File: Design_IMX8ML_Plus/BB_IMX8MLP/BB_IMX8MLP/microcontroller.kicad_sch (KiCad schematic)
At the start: 0 parts

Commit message: Review
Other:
- note added: "Memeoria EEPROM PWM CAN I2C SPI UART"
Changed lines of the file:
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@@
 	(generator_version "8.0")
 	(paper "A4")
+	(text "Memeoria EEPROM\nPWM \nCAN\nI2C\nSPI\nUART"
+		(exclude_from_sim no)
+		(at 72.136 56.642 0)
+		(effects
+			(font
+				(size 5 5)
+			)
+		)
+	)
 )

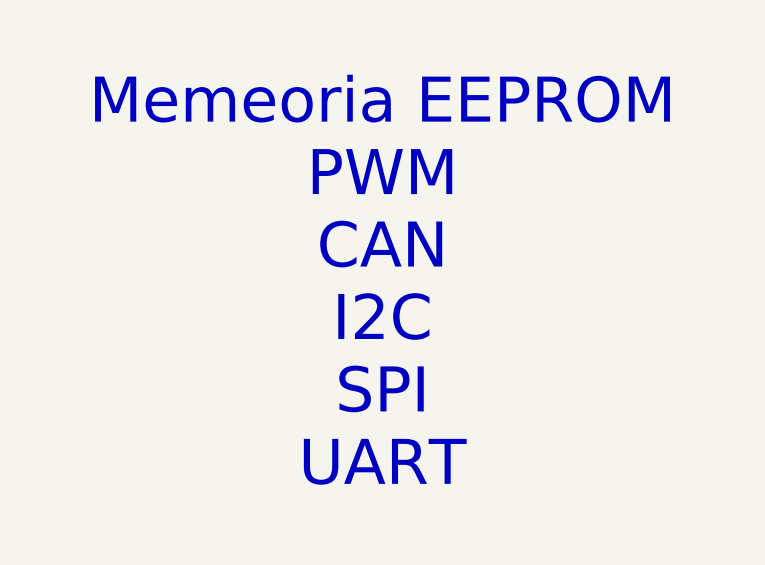
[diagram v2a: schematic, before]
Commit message: reorganization of the componentes
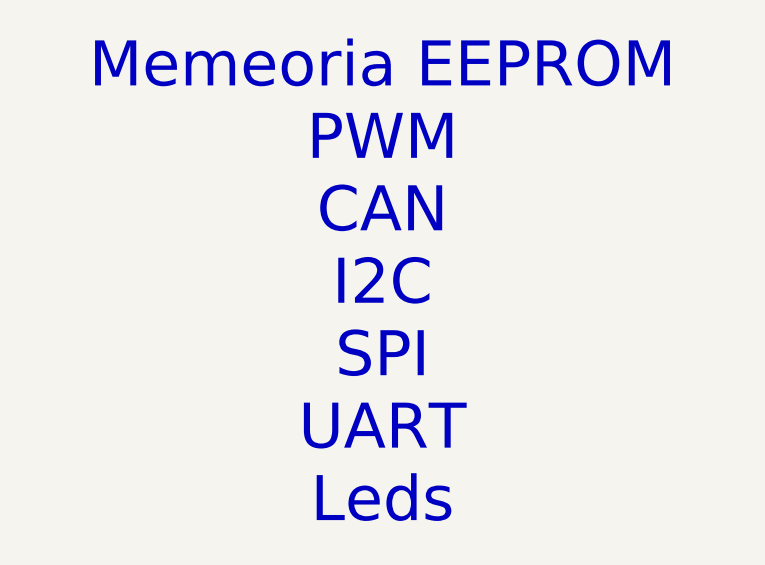
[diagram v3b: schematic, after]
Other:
- note added: "Memeoria EEPROM PWM CAN I2C SPI UART Leds"
- note removed: "Memeoria EEPROM PWM CAN I2C SPI UART"
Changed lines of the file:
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@@
 	(generator_version "8.0")
 	(paper "A4")
-	(text "Memeoria EEPROM\nPWM \nCAN\nI2C\nSPI\nUART"
+	(text "Memeoria EEPROM\nPWM \nCAN\nI2C\nSPI\nUART\nLeds"
 		(exclude_from_sim no)
 		(at 72.136 56.642 0)

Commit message: CPU Board actualizate
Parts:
- added C189, C190, C191, C192: 12Pf, Capacitor_SMD:C_0402_1005Metric, symbol Device:C_Small
- added C193: 100nF, Capacitor_SMD:C_0402_1005Metric, symbol Device:C_Small
- added J16: PB0, Connector_PinHeader_2.54mm:PinHeader_2x10_P2.54mm_Vertical, symbol Connector_Generic:Conn_02x10_Odd_Even
- added R82, R83: 100K, Resistor_SMD:R_0402_1005Metric, symbol Device:R_Small
- added SW4: NRST, Button_Switch_SMD:SW_SPST_TL3342, symbol Switch:SW_Push_Dual
- added SW5: BOOT0, Button_Switch_SMD:SW_SPST_TL3342, symbol Switch:SW_Push_Dual
- added U26: STM32H523CCUx, Package_DFN_QFN:QFN-48-1EP_7x7mm_P0.5mm_EP5.6x5.6mm, symbol MCU_ST_STM32H5:STM32H523CCUx
- added U27: CAT250xxx-HU4, Package_DFN_QFN:DFN-8-1EP_3x2mm_P0.5mm_EP1.75x1.45mm, symbol Memory_EEPROM:CAT250xxx-HU4
- added Y4, Y5: 25MHz, Crystal:Crystal_SMD_0603-4Pin_6.0x3.5mm, symbol Device:Crystal_GND24_Small
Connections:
- new net: C189.1, Y4.1
- new net: C191.1, Y5.1
- new net: C192.1, Y5.3
- new net: U27.4 (GND), U27.9 (GND)
- new net: SW5.1, SW5.3
- new net: U26.24 (VDD), U26.48 (VDD)
- new net: C193.1, R82.2, SW4.1, SW4.3
- new net: C190.1, Y4.3
- new net BOOT0: R83.1, SW5.2, SW5.4, U26.44 (BOOT0)
- new net GND: C189.2, C190.2, C191.2, C192.2, C193.2, R83.2, U26.23 (VSS), U26.35 (VSS), U26.47 (VSS), U26.49 (VSS), U26.8 (VSSA), Y4.2, Y4.4, Y5.2, Y5.4
- new net NRST: SW4.2, SW4.4, U26.7 (NRST)
- new net PB0: J16.4 (Pin_4), U26.18 (PB0)
- new net PB1: J16.3 (Pin_3), U26.19 (PB1)
- new net PB10: J16.14 (Pin_14), U26.21 (PB10)
- new net PB12: J16.16 (Pin_16), U26.25 (PB12)
- new net PB13: J16.15 (Pin_15), U26.26 (PB13)
- new net PB14: J16.18 (Pin_18), U26.27 (PB14)
- new net PB15: J16.17 (Pin_17), U26.28 (PB15)
- new net PB2: J16.6 (Pin_6), U26.20 (PB2)
- new net PB3: J16.5 (Pin_5), U26.39 (PB3(JTDO)
- new net PB4: J16.8 (Pin_8), U26.40 (PB4(NJTRST))
- new net PB5: J16.7 (Pin_7), U26.41 (PB5)
- new net PB6: J16.10 (Pin_10), U26.42 (PB6)
- new net PB7: J16.9 (Pin_9), U26.43 (PB7)
- new net PB8: J16.12 (Pin_12), U26.45 (PB8)
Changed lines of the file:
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@@
 	(generator_version "8.0")
 	(paper "A4")
-	(text "Memeoria EEPROM\nPWM \nCAN\nI2C\nSPI\nUART\nLeds"
-		(exclude_from_sim no)
-		(at 72.136 56.642 0)
-		(effects
-			(font
-				(size 5 5)
-			)
-		)
-	)
-)

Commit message: [PROCESSOR] Create zones It added power zones in the four layer
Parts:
- added J3: boot, Connector_PinHeader_2.54mm:PinHeader_1x04_P2.54mm_Vertical_SMD_Pin1Right, symbol Connector_Generic:Conn_02x02_Odd_Even
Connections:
- net GND: now also J16.19 (Pin_19), J16.20 (Pin_20)
- net at U26.12 (PA2): now also J3.1 (Pin_1)
- net at U26.13 (PA3): now also J3.3 (Pin_3)
- net jtag_Rx: now reaches U26.30 (PA9)
- net jtag_Tx: now reaches U26.31 (PA10)
- net USB_D-: now reaches U26.32 (PA11)
- net USB_D+: now reaches U26.33 (PA12)
- new net boot_Rx: J3.2 (Pin_2)
- new net boot_Tx: J3.4 (Pin_4)

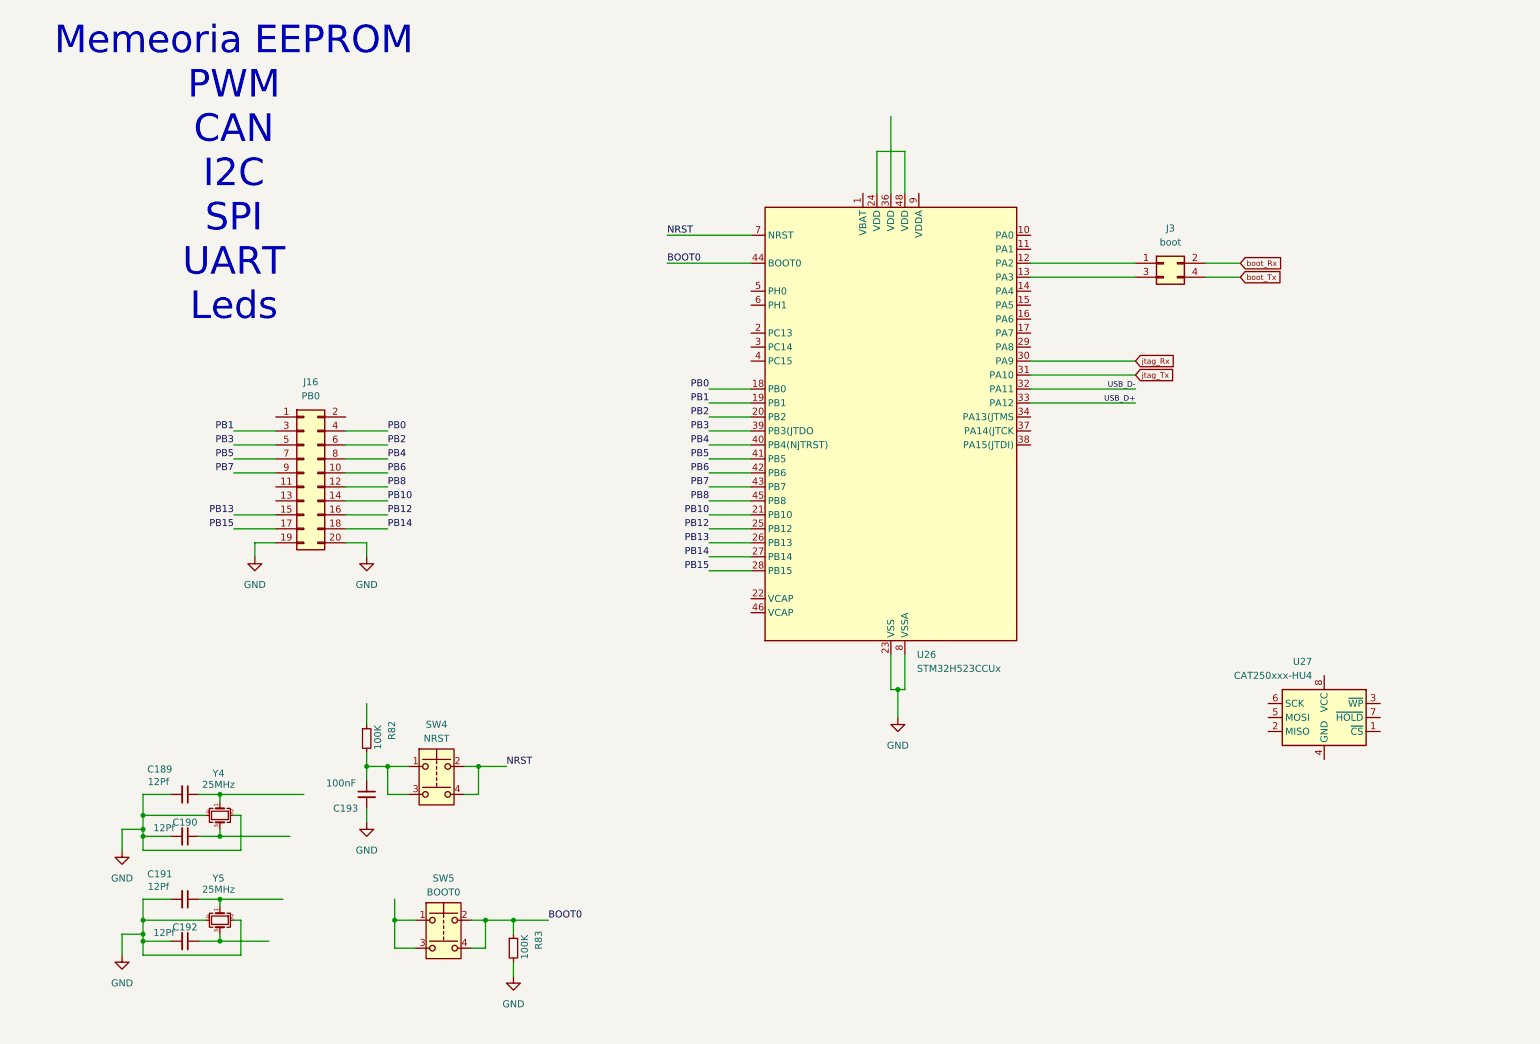
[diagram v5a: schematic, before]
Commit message: [BB_IMX8MLP IMX8MLP] Actuallizated to 9.0 kicad version
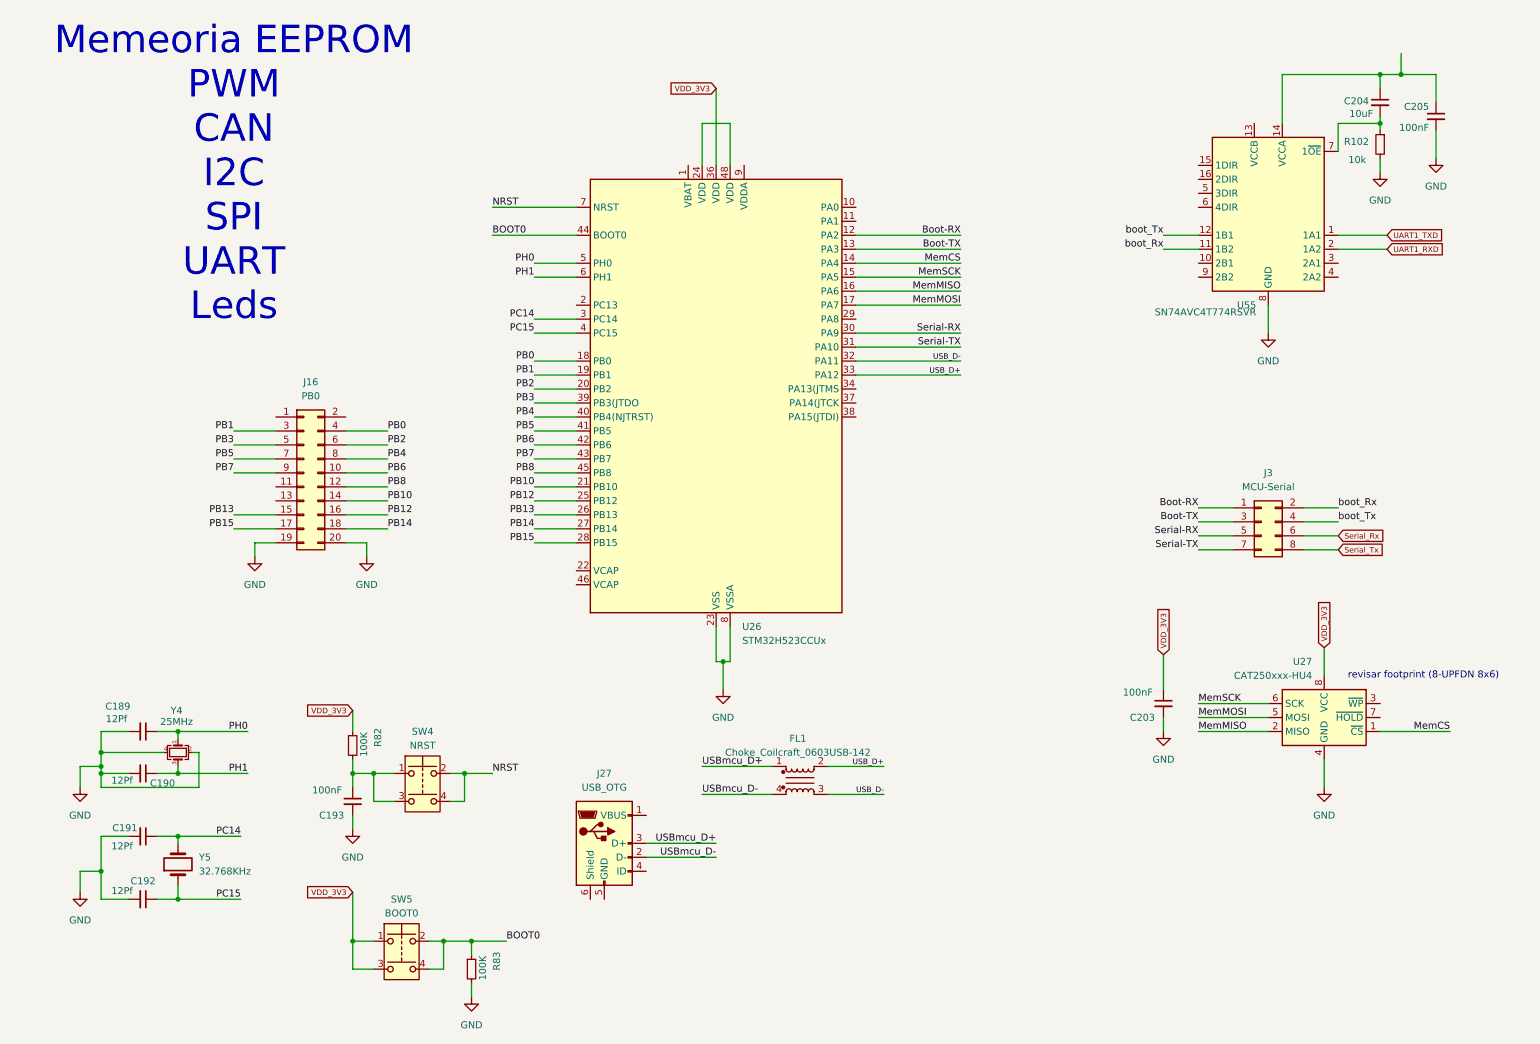
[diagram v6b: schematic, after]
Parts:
- removed J3: boot, Connector_PinHeader_2.54mm:PinHeader_1x04_P2.54mm_Vertical_SMD_Pin1Right, symbol Connector_Generic:Conn_02x02_Odd_Even
- removed Y5: 25MHz, Crystal:Crystal_SMD_0603-4Pin_6.0x3.5mm, symbol Device:Crystal_GND24_Small
- added C203, C205: 100nF, Capacitor_SMD:C_0402_1005Metric, symbol Device:C_Small
- added C204: 10uF, Capacitor_SMD:C_0402_1005Metric, symbol Device:C_Small
- added FL1: Choke_Coilcraft_0603USB-142, Inductor_SMD:L_CommonModeChoke_Coilcraft_0603USB, symbol Filter:Choke_Coilcraft_0603USB-142
- added J27: USB_OTG, Connector_USB:USB_Mini-B_Lumberg_2486_01_Horizontal, symbol Connector:USB_OTG
- added J3: MCU-Serial, Connector_PinHeader_2.54mm:PinHeader_2x04_P2.54mm_Vertical, symbol Connector_Generic:Conn_02x04_Odd_Even
- added R102: 10k, Resistor_SMD:R_0402_1005Metric, symbol Device:R_Small
- added U55: SN74AVC4T774RSVR, Package_DFN_QFN:UQFN-16_1.8x2.6mm_P0.4mm, symbol _W_MX8M:SN74AVC4T774RSVR
- added Y5: 32.768KHz, Crystal:Crystal_SMD_3215-2Pin_3.2x1.5mm, symbol Device:Crystal
- C189, C190, C191, C192: MP (none) -> C0402C120D5GACTU; Price (none) -> 0.5
- C193: MP (none) -> C0402C104K4RACTU; Price (none) -> 0.1
- R82, R83: MP (none) -> RC0402JR-07100KL; Price (none) -> 0.1
- U26: MP (none) -> STM32H523CCU6; Price (none) -> 4.5
- U27: MP (none) -> MT29F4G01ABAFDWB-IT:F TR; Price (none) -> 4
- Y4: footprint Crystal:Crystal_SMD_0603-4Pin_6.0x3.5mm -> Crystal:Crystal_SMD_3225-4Pin_3.2x2.5mm; MP (none) -> TSX-3225 25.0000MF15X-AS3; Price (none) -> 1.5
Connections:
- net GND: now also U27.4 (GND), U27.9 (GND), C203.2, C205.2, R102.2, U55.8 (GND)
- net USB_D+: now also FL1.2
- net USB_D-: now also FL1.3
- net boot_Rx: now also J3.2 (Pin_2), U55.11 (1B2)
- net boot_Tx: now also J3.4 (Pin_4), U55.12 (1B1)
- net PH0: now reaches C189.1, Y4.1
- net PH0: now also U26.5 (PH0)
- net PC14: now reaches C191.1
- net PC14: now also U26.3 (PC14), Y5.2
- net PC15: now reaches C192.1
- net PC15: now also U26.4 (PC15), Y5.1
- net MemCS: now reaches U27.1 (~{CS})
- net MemCS: now also U26.14 (PA4)
- net MemMISO: now reaches U27.2 (MISO)
- net MemMISO: now also U26.16 (PA6)
- net MemMOSI: now reaches U27.5 (MOSI)
- net MemMOSI: now also U26.17 (PA7)
- net MemSCK: now reaches U27.6 (SCK)
- net MemSCK: now also U26.15 (PA5)
- net VDD_3V3: now reaches U27.8 (VCC)
- net VDD_3V3: now also R82.1, SW5.1, SW5.3, U26.36 (VDD), C203.1
- net Boot-RX: now reaches U26.12 (PA2)
- net Boot-RX: now also J3.1 (Pin_1)
- net Boot-TX: now reaches U26.13 (PA3)
- net Boot-TX: now also J3.3 (Pin_3)
- net PH1: now reaches U26.6 (PH1)
- net PH1: now also C190.1, Y4.3
- net jtag_Rx renamed Serial-RX
- net Serial-RX: now also J3.5 (Pin_5)
- net jtag_Tx renamed Serial-TX
- net Serial-TX: now also J3.7 (Pin_7)
- new net: C204.1, C205.1, U55.14 (VCCA)
- new net: C204.2, R102.1, U55.7 (1~{OE})
- new net Serial_Rx: J3.6 (Pin_6)
- new net Serial_Tx: J3.8 (Pin_8)
- new net UART1_RXD: U55.2 (1A2)
- new net UART1_TXD: U55.1 (1A1)
- new net USBmcu_D+: FL1.1, J27.3 (D+)
- new net USBmcu_D-: FL1.4, J27.2 (D-)
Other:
- note added: "revisar footprint (8-UPFDN 8x6)"
- moved on the sheet: C189, C190, C191, C192, C193, R82, R83, SW4, SW5, U26, Y4
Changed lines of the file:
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@@
 (kicad_sch
-	(version 20231120)
+	(version 20250114)
 	(generator "eeschema")
-	(generator_version "8.0")
+	(generator_version "9.0")
 	(paper "A4")

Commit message: [LoRa] Starting a new project
Starting a new project base on LoRa LR1121, this project use
the module LBAA0XV2GT-001 that had sub-GHz and 2.4GHz frequencies.
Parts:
- removed FL1: Choke_Coilcraft_0603USB-142, Inductor_SMD:L_CommonModeChoke_Coilcraft_0603USB, symbol Filter:Choke_Coilcraft_0603USB-142
- added U57: PCMF1USB3SZ, _W_SBC:WLCSP52-1-2_NEX, symbol _W_MX8M:PCMF1HDMI2S
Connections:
- net GND: now also J27.5 (GND), U57.B1 (GND_CH1)
- net USB_D+: now also U57.C1 (CH1_OUT+)
- net USB_D-: now also U57.C2 (CH1_OUT-)
- net USBmcu_D+: now also U57.A1 (CH1_IN+)
- net USBmcu_D-: now also U57.A2 (CH1_IN-)
- net boot_Tx: no longer U55.12 (1B1)
- new net Boot_Tx: U55.12 (1B1)
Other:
- moved on the sheet: R83, SW5
